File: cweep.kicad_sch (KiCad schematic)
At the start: 51 parts

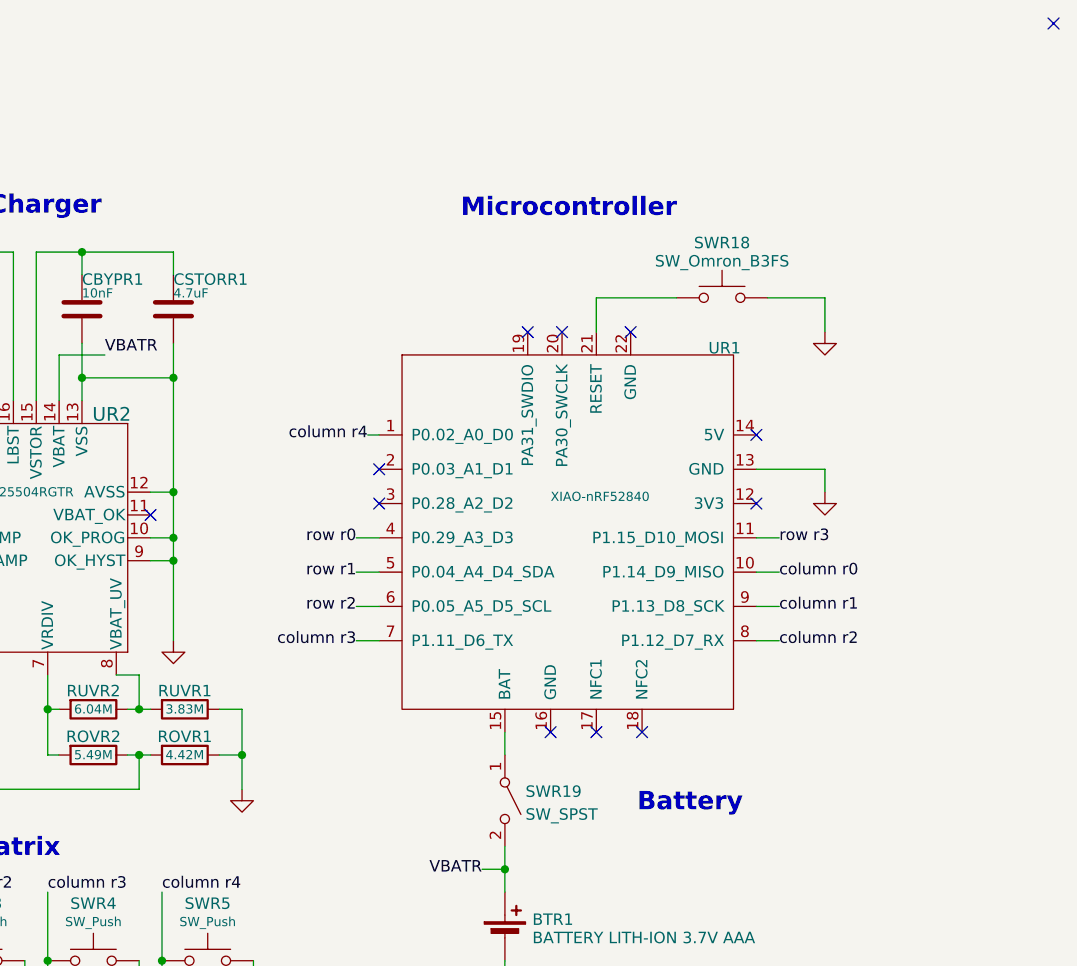
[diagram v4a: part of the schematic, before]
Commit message: fix: minor footprint and label alignments
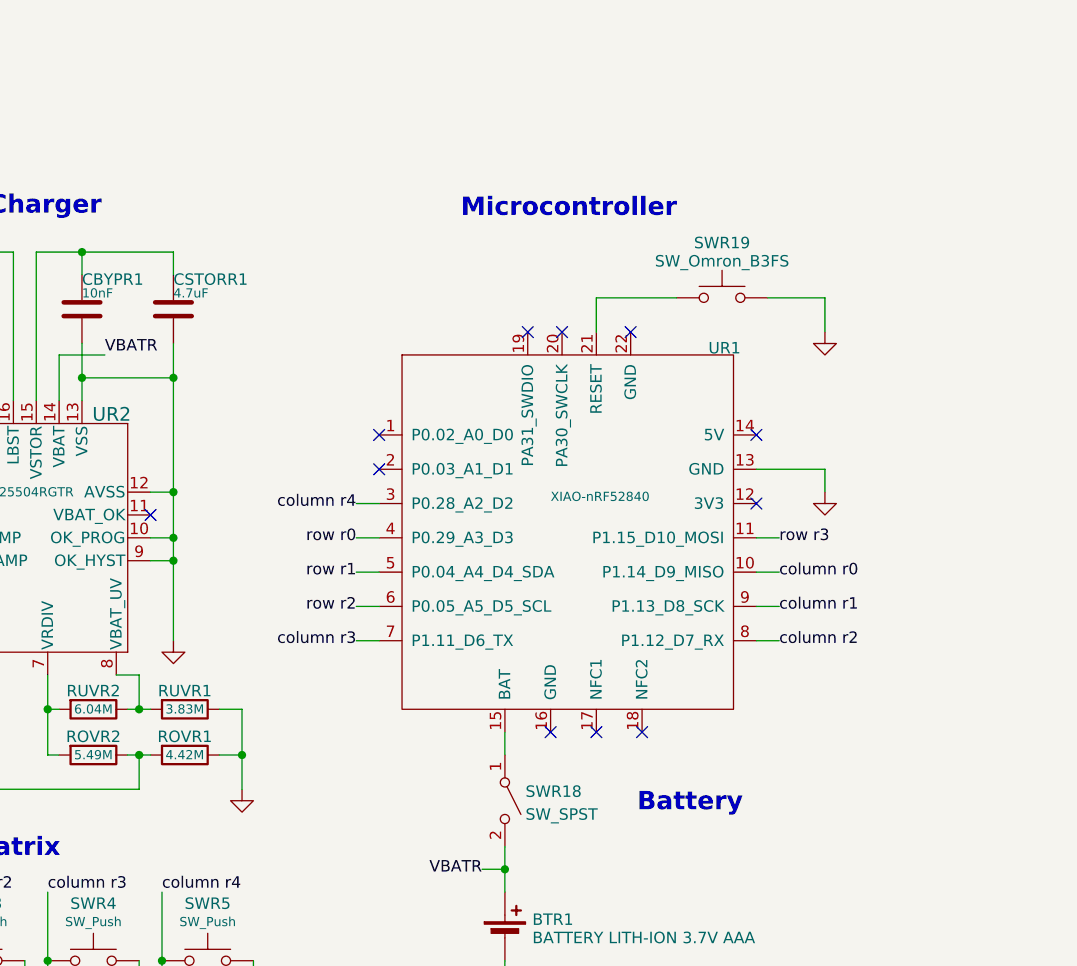
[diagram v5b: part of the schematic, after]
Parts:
- renumbered SWR19 to SWR18, SWR18 to SWR19
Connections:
- net column r4: now also UR1.3 (P0.28_A2_D2); no longer UR1.1 (P0.02_A0_D0)
- no-connect marks 12 -> 11
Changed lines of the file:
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@@
 	)
 	(no_connect
-		(at 300.99 -2.54)
-	)
-	(no_connect
 		(at 246.38 31.75)
 	)
 	(no_connect
-		(at 226.06 50.8)
+		(at 226.06 43.18)
 	)
 	(wire
@@
 	(wire
 		(pts
+			(xy 223.52 50.8) (xy 226.06 50.8)
+		)
+		(stroke
+			(width 0)
+			(type default)
+		)
+	)
+	(wire
+		(pts
 			(xy 203.2 54.61) (xy 203.2 57.15)
 		)
@@
 	(wire
 		(pts
-			(xy 224.79 43.18) (xy 226.06 43.18)
-		)
-		(stroke
-			(width 0)
-			(type default)
-		)
-	)
-	(wire
-		(pts
 			(xy 161.29 128.27) (xy 173.99 128.27)
 		)
@@
 	)
 	(label "column r4"
-		(at 224.79 43.18 180)
+		(at 223.52 50.8 180)
 		(effects
 			(font
@@
 	)
 	(symbol
-		(lib_id "power:GND")
-		(at 203.2 66.04 0)
-		(mirror y)
-		(unit 1)
-		(exclude_from_sim no)
-		(in_bom yes)
-		(on_board yes)
-		(dnp no)
-		(property "Reference" "#PWR01"
-			(at 203.2 72.39 0)
-			(effects
-				(font
-					(size 1.27 1.27)
-				)
-				(hide yes)
-			)
-		)
-		(property "Value" "GND"
-			(at 203.2 71.12 0)
-			(effects
-				(font
-					(size 1.27 1.27)
-				)
-				(hide yes)
-			)
-		)
-		(property "Footprint" ""
-			(at 203.2 66.04 0)
-			(effects
-				(font
-					(size 1.27 1.27)
-				)
-				(hide yes)
-			)
-		)
-		(property "Datasheet" ""
-			(at 203.2 66.04 0)
-			(effects
-				(font
-					(size 1.27 1.27)
-				)
-				(hide yes)
-			)
-		)
-		(property "Description" "Power symbol creates a global label with name \"GND\" , ground"
-			(at 203.2 66.04 0)
-			(effects
-				(font
-					(size 1.27 1.27)
-				)
-				(hide yes)
-			)
-		)
-		(pin "1"
-		)
-		(instances
-			(project ""
-				(path "/639fa181-da29-4b09-bbdd-4ee6b511df9a"
-					(reference "#PWR01")
-					(unit 1)
-				)
-			)
-		)
-	)
-	(symbol
 		(lib_id "Switch:SW_SPST")
 		(at 240.03 83.82 270)
@@
 		(on_board yes)
 		(dnp no)
-		(property "Reference" "SWR19"
+		(property "Reference" "SWR18"
 			(at 242.316 82.804 90)
 			(effects
@@
 			(project ""
 				(path "/639fa181-da29-4b09-bbdd-4ee6b511df9a"
-					(reference "SWR19")
+					(reference "SWR18")
 					(unit 1)
 				)
@@
 		(on_board yes)
 		(dnp no)
-		(property "Reference" "SWR18"
+		(property "Reference" "SWR19"
 			(at 264.16 21.844 0)
 			(effects
@@
 			(project ""
 				(path "/639fa181-da29-4b09-bbdd-4ee6b511df9a"
-					(reference "SWR18")
+					(reference "SWR19")
 					(unit 1)
 				)
@@
 					(unit 1)
 				)
+			)
+		)
+	)
+	(symbol
+		(lib_id "power:GND")
+		(at 203.2 66.04 0)
+		(unit 1)
+		(exclude_from_sim no)
+		(in_bom yes)
+		(on_board yes)
+		(dnp no)
+		(property "Reference" "#PWR01"
+			(at 203.2 72.39 0)
+			(effects
+				(font
+					(size 1.27 1.27)
+				)
+				(hide yes)
+			)
+		)
+		(property "Value" "GND"
+			(at 203.2 69.596 0)
+			(effects
+				(font
+					(size 1.016 1.016)
+				)
+				(hide yes)
+			)
+		)
+		(property "Footprint" ""
+			(at 203.2 66.04 0)
+			(effects
+				(font
+					(size 1.27 1.27)
+				)
+				(hide yes)
+			)
+		)
+		(property "Datasheet" ""
+			(at 203.2 66.04 0)
+			(effects
+				(font
+					(size 1.27 1.27)
+				)
+				(hide yes)
+			)
+		)
+		(property "Description" "Power symbol creates a global label with name \"GND\" , ground"
+			(at 203.2 66.04 0)
+			(effects
+				(font
+					(size 1.27 1.27)
+				)
+				(hide yes)
+			)
+		)
+		(pin "1"
+		)
+		(instances
+			(project "cweep"
+				(path "/639fa181-da29-4b09-bbdd-4ee6b511df9a"
+					(reference "#PWR01")
+					(unit 1)
+				)

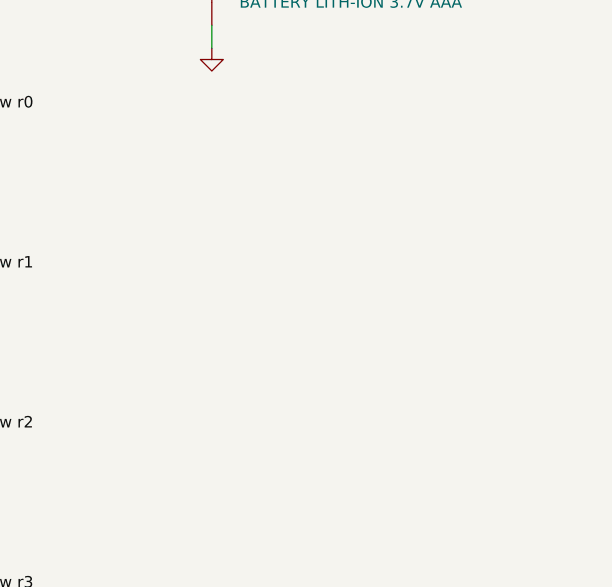
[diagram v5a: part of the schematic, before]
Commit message: feat: add case mounting holes
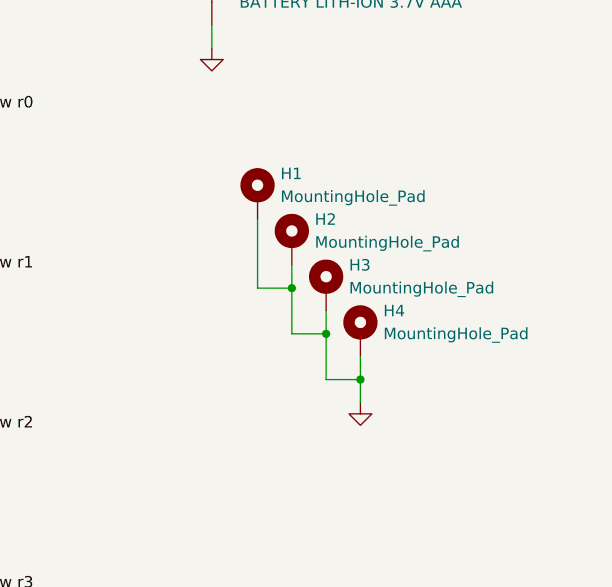
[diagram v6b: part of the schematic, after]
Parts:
- added H1, H2, H3, H4: MountingHole_Pad, MountingHole:MountingHole_2.5mm_Pad, symbol Mechanical:MountingHole_Pad
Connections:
- net GND: now also H1.1, H2.1, H3.1, H4.1

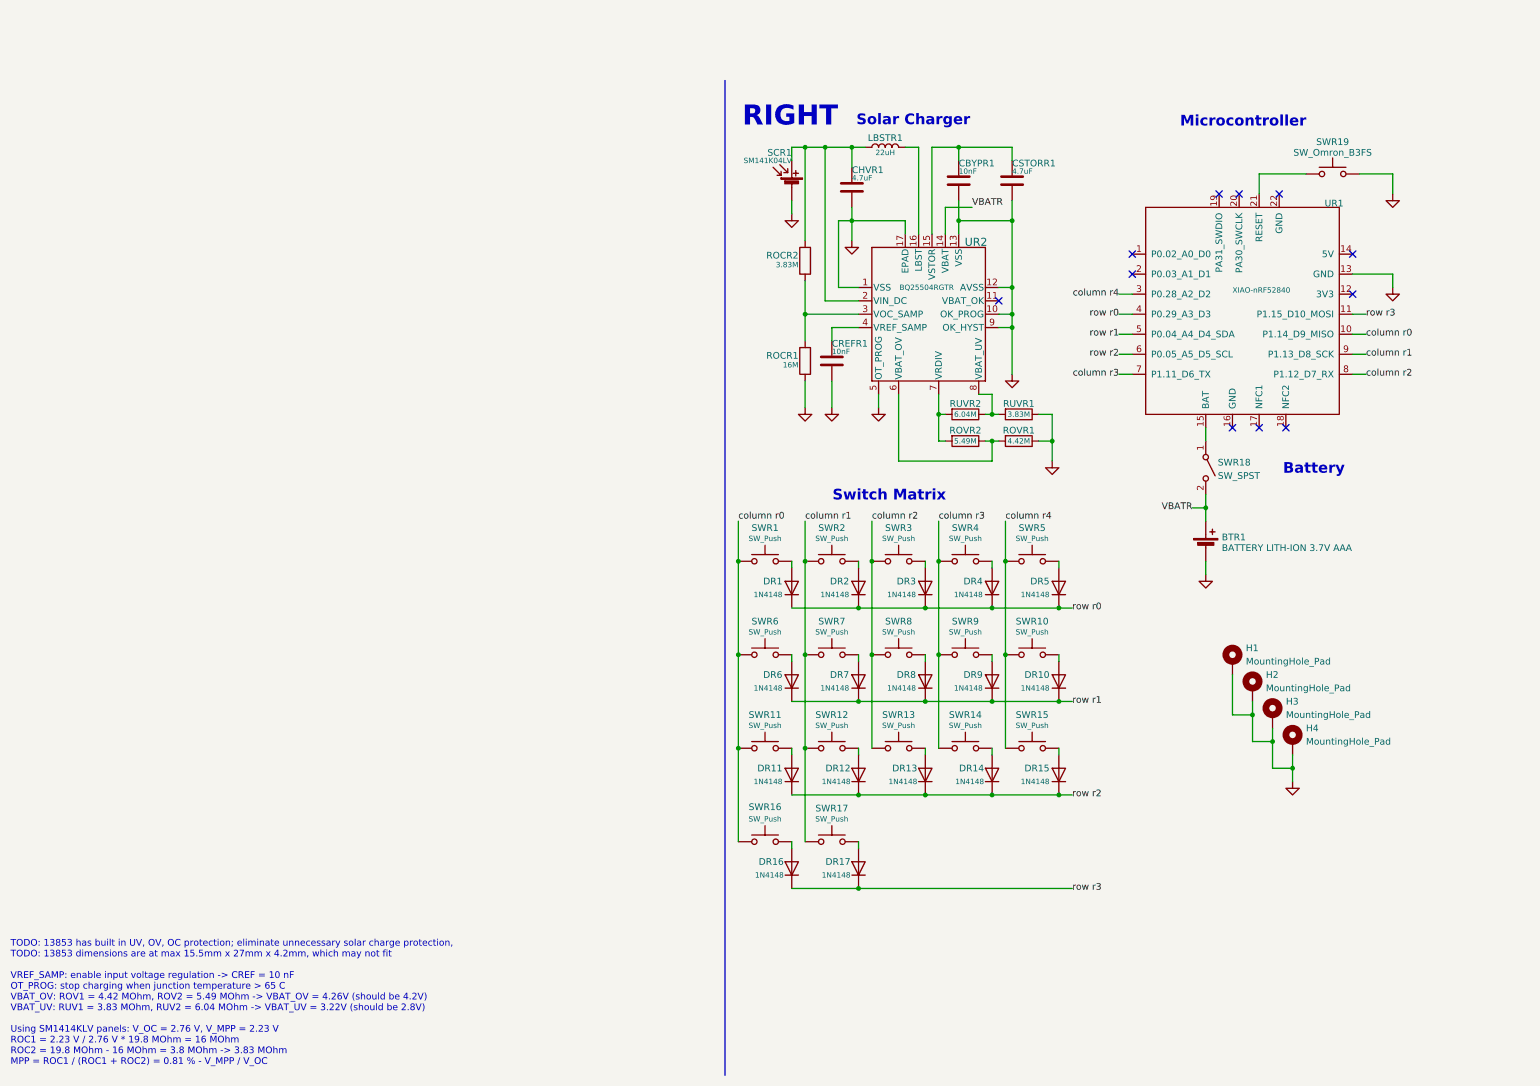
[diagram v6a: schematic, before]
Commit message: feat: 2.5mm -> 2.2mm mounting holes
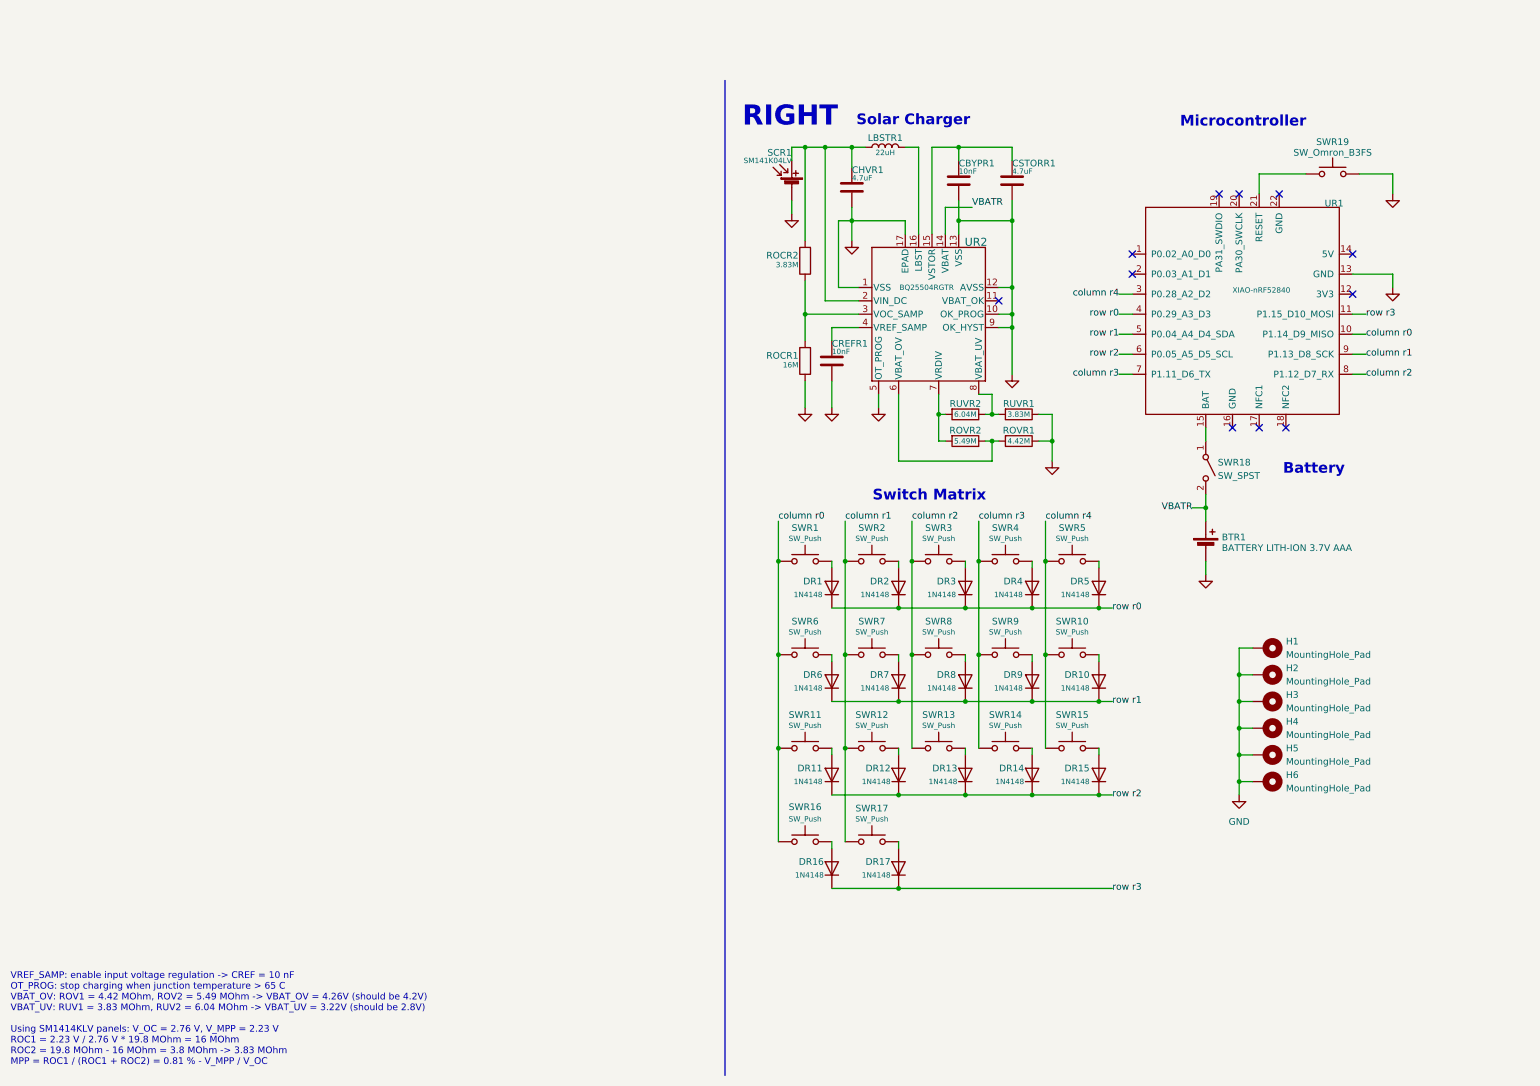
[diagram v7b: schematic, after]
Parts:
- added H5, H6: MountingHole_Pad, MountingHole:MountingHole_2.2mm_M2_DIN965_Pad_TopOnly, symbol Mechanical:MountingHole_Pad
- H1, H2, H3, H4: footprint MountingHole:MountingHole_2.5mm_Pad -> MountingHole:MountingHole_2.2mm_M2_DIN965_Pad_TopOnly
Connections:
- net GND: now also H5.1, H6.1
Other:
- note added: "VREF_SAMP: enable input voltage regulation -> CREF = 10 nF OT_PROG: stop charging when junction temperature > 65 C VBAT_OV: ROV1 = 4.42 MOhm, ROV2 = 5.49 MOhm -> VBAT_OV = 4.26V (should be 4.2V) VBAT_UV: RUV1 = 3.83 MOhm, RUV2 = 6.04 MOhm -> VBAT_UV = 3.22V (should be 2.8V) Using SM1414KLV panels: V_OC = 2.76 V, V_MPP = 2.23 V ROC1 = 2.23 V / 2.76 V * 19.8 MOhm = 16 MOhm ROC2 = 19.8 MOhm - 16 MOh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"
- note removed: "TODO: 13853 has built in UV, OV, OC protection; eliminate unnecessary solar charge protection, TODO: 13853 dimensions are at max 15.5mm x 27mm x 4.2mm, which may not fit VREF_SAMP: enable input voltage regulation -> CREF = 10 nF OT_PROG: stop charging when junction temperature > 65 C VBAT_OV: ROV1 = 4.42 MOhm, ROV2 = 5.49 MOhm -> VBAT_OV = 4.26V (should be 4.2V) VBAT_UV: RUV1 = 3.83 MOhm, RUV2 = 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"
- moved on the sheet: DR1, DR10, DR11, DR12, DR13, DR14, DR15, DR16, DR17, DR2, DR3, DR4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

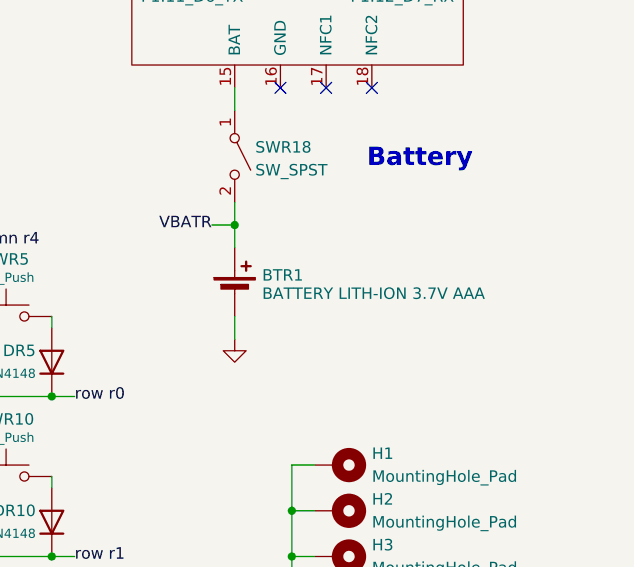
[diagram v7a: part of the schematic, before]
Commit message: fix: join solar ground zone and avoid silkscreen clipping
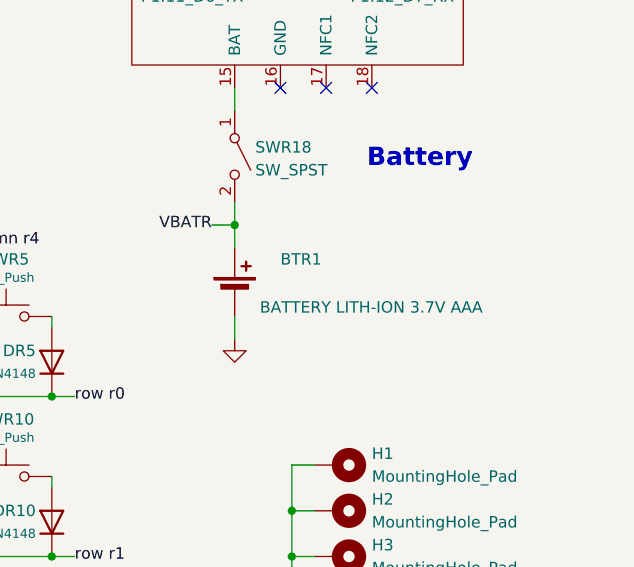
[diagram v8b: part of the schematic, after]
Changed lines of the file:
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@@
 		(dnp no)
 		(property "Reference" "BTR1"
-			(at 243.078 97.028 0)
+			(at 245.11 95.25 0)
 			(effects
 				(font
@@
 			)
 		)
-		(property "Value" "BATTERY LITH-ION 3.7V AAA"
-			(at 243.078 99.06 0)
+		(property "Value" "BATTERY\nLITH-ION\n3.7V\nAAA"
+			(at 242.824 100.584 0)
 			(effects
 				(font
